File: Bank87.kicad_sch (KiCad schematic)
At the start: 1 part, among them U1 XCKU5P-FFVB676

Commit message: <feat>: Modified Power Tree
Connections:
- net FAN_PWM: no longer U1.J15 (IO_L4P_AD12P_87)
- net 3V3 renamed VCCO_HD87
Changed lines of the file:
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@@
 	(wire
 		(pts
-			(xy 105.41 77.47) (xy 107.95 77.47)
+			(xy 107.95 69.85) (xy 105.41 69.85)
 		)
 		(stroke
@@
 	(wire
 		(pts
-			(xy 107.95 69.85) (xy 105.41 69.85)
+			(xy 64.77 116.84) (xy 64.77 118.11)
 		)
 		(stroke
@@
 	(wire
 		(pts
-			(xy 67.31 116.84) (xy 67.31 118.11)
+			(xy 64.77 118.11) (xy 67.31 118.11)
 		)
 		(stroke
@@
 	(global_label "FAN_PWM"
 		(shape input)
-		(at 107.95 77.47 0)
+		(at 119.38 77.47 0)
 		(fields_autoplaced yes)
 		(effects
@@
 		)
 		(property "Intersheetrefs" "${INTERSHEET_REFS}"
-			(at 119.5833 77.47 0)
+			(at 131.0133 77.47 0)
 			(hide yes)
 			(show_name no)
@@
 				)
 				(justify left)
-			)
-		)
-	)
-	(symbol
-		(lib_id "dfdtc_power:+1V8")
-		(at 67.31 116.84 0)
-		(unit 1)
-		(body_style 1)
-		(exclude_from_sim no)
-		(in_bom yes)
-		(on_board yes)
-		(in_pos_files yes)
-		(dnp no)
-		(property "Reference" "#PWR094"
-			(at 67.31 120.65 0)
-			(hide yes)
-			(show_name no)
-			(do_not_autoplace no)
-			(effects
-				(font
-					(size 1.27 1.27)
-				)
-			)
-		)
-		(property "Value" "3V3"
-			(at 67.31 112.522 0)
-			(show_name no)
-			(do_not_autoplace no)
-			(effects
-				(font
-					(size 1.27 1.27)
-				)
-			)
-		)
-		(property "Footprint" ""
-			(at 67.31 116.84 0)
-			(hide yes)
-			(show_name no)
-			(do_not_autoplace no)
-			(effects
-				(font
-					(size 1.27 1.27)
-				)
-			)
-		)
-		(property "Datasheet" ""
-			(at 67.31 116.84 0)
-			(hide yes)
-			(show_name no)
-			(do_not_autoplace no)
-			(effects
-				(font
-					(size 1.27 1.27)
-				)
-			)
-		)
-		(property "Description" "Power symbol creates a global label with name \"+1V8\""
-			(at 67.31 116.84 0)
-			(hide yes)
-			(show_name no)
-			(do_not_autoplace no)
-			(effects
-				(font
-					(size 1.27 1.27)
-				)
-			)
-		)
-		(pin "1"
-		)
-		(instances
-			(project "KU5P_Core"
-				(path "/68d0ebd3-4770-4e42-a15d-94722405f64d/8a27e5b5-485e-4923-a8ca-92c1e43f1f46/460e3070-2dd4-4116-b69c-9f64446c5546/1cc1f301-f9be-4549-96f2-e34678c8efe7/e17dbfff-d0b7-409b-9b0d-db23be06c6a9"
-					(reference "#PWR094")
-					(unit 1)
-				)
 			)
 		)
@@
 				)
 			)
+		)
+	)
+	(symbol
+		(lib_id "dfdtc_power:+1V8")
+		(at 64.77 116.84 0)
+		(unit 1)
+		(body_style 1)
+		(exclude_from_sim no)
+		(in_bom yes)
+		(on_board yes)
+		(in_pos_files yes)
+		(dnp no)
+		(fields_autoplaced yes)
+		(property "Reference" "#PWR0198"
+			(at 64.77 120.65 0)
+			(hide yes)
+			(show_name no)
+			(do_not_autoplace no)
+			(effects
+				(font
+					(size 1.27 1.27)
+				)
+			)
+		)
+		(property "Value" "VCCO_HD87"
+			(at 64.77 111.76 0)
+			(show_name no)
+			(do_not_autoplace no)
+			(effects
+				(font
+					(size 1.27 1.27)
+				)
+			)
+		)
+		(property "Footprint" ""
+			(at 64.77 116.84 0)
+			(hide yes)
+			(show_name no)
+			(do_not_autoplace no)
+			(effects
+				(font
+					(size 1.27 1.27)
+				)
+			)
+		)
+		(property "Datasheet" ""
+			(at 64.77 116.84 0)
+			(hide yes)
+			(show_name no)
+			(do_not_autoplace no)
+			(effects
+				(font
+					(size 1.27 1.27)
+				)
+			)
+		)
+		(property "Description" "Power symbol creates a global label with name \"+1V8\""
+			(at 64.77 116.84 0)
+			(hide yes)
+			(show_name no)
+			(do_not_autoplace no)
+			(effects
+				(font
+					(size 1.27 1.27)
+				)
+			)
+		)
+		(pin "1"
+		)
+		(instances
+			(project "KU5P_Core"
+				(path "/68d0ebd3-4770-4e42-a15d-94722405f64d/8a27e5b5-485e-4923-a8ca-92c1e43f1f46/460e3070-2dd4-4116-b69c-9f64446c5546/1cc1f301-f9be-4549-96f2-e34678c8efe7/e17dbfff-d0b7-409b-9b0d-db23be06c6a9"
+					(reference "#PWR0198")
+					(unit 1)
+				)
+			)

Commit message: finishing schematic
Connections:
- net FAN_PWM: now also U1.J15 (IO_L4P_AD12P_87_P)
- net IO_L11N_AD9N_87_N: now reaches U1.A12 (IO_L11N_AD9N_87_N)
- net IO_L11P_AD9P_87_P: now reaches U1.A13 (IO_L11P_AD9P_87_P)
- net IO_L12N_AD8N_87_N: now reaches U1.A14 (IO_L12N_AD8N_87_N)
- net IO_L10N_AD10N_87_N: now reaches U1.B12 (IO_L10N_AD10N_87_N)
- net IO_L12P_AD8P_87_P: now reaches U1.B14 (IO_L12P_AD8P_87_P)
- net IO_L10P_AD10P_87_P: now reaches U1.C12 (IO_L10P_AD10P_87_P)
- net IO_L9N_AD11N_87_N: now reaches U1.C13 (IO_L9N_AD11N_87_N)
- net IO_L9P_AD11P_87_P: now reaches U1.C14 (IO_L9P_AD11P_87_P)
- net IO_L8N_HDGC_87_N: now reaches U1.D13 (IO_L8N_HDGC_87_N)
- net IO_L8P_HDGC_87_P: now reaches U1.D14 (IO_L8P_HDGC_87_P)
- net IO_L7N_HDGC_87_N: now reaches U1.E12 (IO_L7N_HDGC_87_N)
- net IO_L7P_HDGC_87_P: now reaches U1.E13 (IO_L7P_HDGC_87_P)
- net FAN_TACH: now reaches U1.F12 (IO_L5N_HDGC_87_N)
- net IO_L6N_HDGC_87_N: now reaches U1.F13 (IO_L6N_HDGC_87_N)
- net PMIC_32KOUT: now reaches U1.F14 (IO_L6P_HDGC_87_P)
- net GTY_AUX_b: now reaches U1.G12 (IO_L5P_HDGC_87_P)
- net GTY_AUX_a: now reaches U1.J14 (IO_L4N_AD12N_87_N)
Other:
- moved on the sheet: U1I

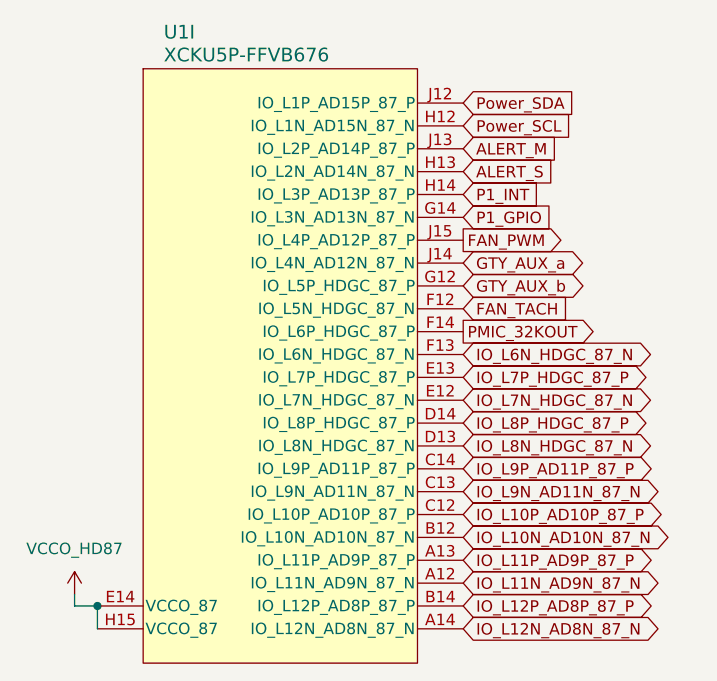
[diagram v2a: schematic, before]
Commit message: change net name to of IO diff pairs, add a scripts for name modification
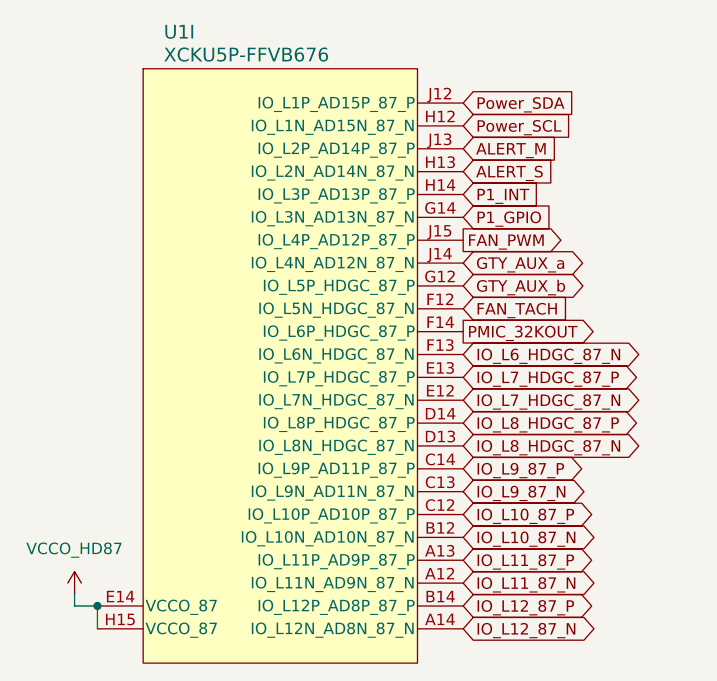
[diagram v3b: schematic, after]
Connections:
- net IO_L10N_AD10N_87_N renamed IO_L10_87_N
- net IO_L10P_AD10P_87_P renamed IO_L10_87_P
- net IO_L11N_AD9N_87_N renamed IO_L11_87_N
- net IO_L11P_AD9P_87_P renamed IO_L11_87_P
- net IO_L12N_AD8N_87_N renamed IO_L12_87_N
- net IO_L12P_AD8P_87_P renamed IO_L12_87_P
- net IO_L6N_HDGC_87_N renamed IO_L6_HDGC_87_N
- net IO_L7N_HDGC_87_N renamed IO_L7_HDGC_87_N
- net IO_L7P_HDGC_87_P renamed IO_L7_HDGC_87_P
- net IO_L8N_HDGC_87_N renamed IO_L8_HDGC_87_N
- net IO_L8P_HDGC_87_P renamed IO_L8_HDGC_87_P
- net IO_L9N_AD11N_87_N renamed IO_L9_87_N
- net IO_L9P_AD11P_87_P renamed IO_L9_87_P
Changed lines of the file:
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@@
 		)
 	)
-	(global_label "IO_L8N_HDGC_87_N"
+	(global_label "IO_L8_HDGC_87_N"
 		(shape bidirectional)
 		(at 107.95 100.33 0)
@@
 		)
 	)
-	(global_label "IO_L11N_AD9N_87_N"
+	(global_label "IO_L11_87_N"
 		(shape bidirectional)
 		(at 107.95 115.57 0)
@@
 		)
 	)
-	(global_label "IO_L8P_HDGC_87_P"
+	(global_label "IO_L8_HDGC_87_P"
 		(shape bidirectional)
 		(at 107.95 97.79 0)
@@
 		)
 	)
-	(global_label "IO_L6N_HDGC_87_N"
+	(global_label "IO_L6_HDGC_87_N"
 		(shape bidirectional)
 		(at 107.95 90.17 0)
@@
 		)
 	)
-	(global_label "IO_L9N_AD11N_87_N"
+	(global_label "IO_L9_87_N"
 		(shape bidirectional)
 		(at 107.95 105.41 0)
@@
 		)
 	)
-	(global_label "IO_L12N_AD8N_87_N"
+	(global_label "IO_L12_87_N"
 		(shape bidirectional)
 		(at 107.95 120.65 0)
@@
 		)
 	)
-	(global_label "IO_L7P_HDGC_87_P"
+	(global_label "IO_L7_HDGC_87_P"
 		(shape bidirectional)
 		(at 107.95 92.71 0)
@@
 		)
 	)
-	(global_label "IO_L10N_AD10N_87_N"
+	(global_label "IO_L10_87_N"
 		(shape bidirectional)
 		(at 107.95 110.49 0)
@@
 		)
 	)
-	(global_label "IO_L12P_AD8P_87_P"
+	(global_label "IO_L12_87_P"
 		(shape bidirectional)
 		(at 107.95 118.11 0)
@@
 		)
 	)
-	(global_label "IO_L11P_AD9P_87_P"
+	(global_label "IO_L11_87_P"
 		(shape bidirectional)
 		(at 107.95 113.03 0)
@@
 		)
 	)
-	(global_label "IO_L10P_AD10P_87_P"
+	(global_label "IO_L10_87_P"
 		(shape bidirectional)
 		(at 107.95 107.95 0)
@@
 		)
 	)
-	(global_label "IO_L9P_AD11P_87_P"
+	(global_label "IO_L9_87_P"
 		(shape bidirectional)
 		(at 107.95 102.87 0)
@@
 		)
 	)
-	(global_label "IO_L7N_HDGC_87_N"
+	(global_label "IO_L7_HDGC_87_N"
 		(shape bidirectional)
 		(at 107.95 95.25 0)
